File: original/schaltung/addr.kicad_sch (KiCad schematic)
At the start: 6 parts

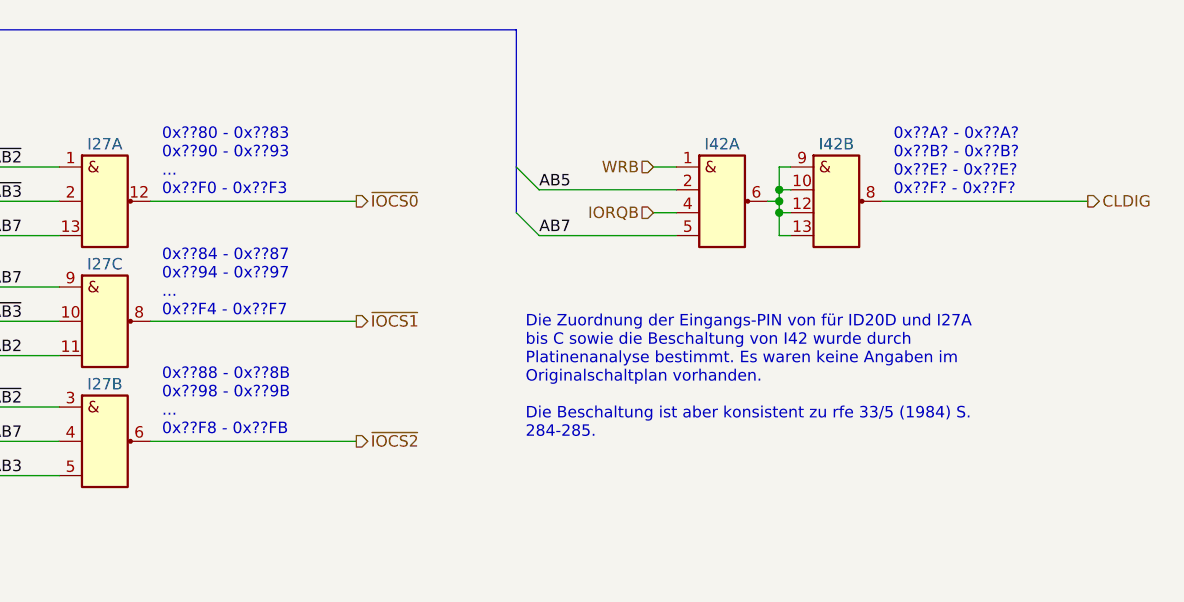
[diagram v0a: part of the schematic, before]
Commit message: I/O-Adressraum auf 8 Bit gekürzt
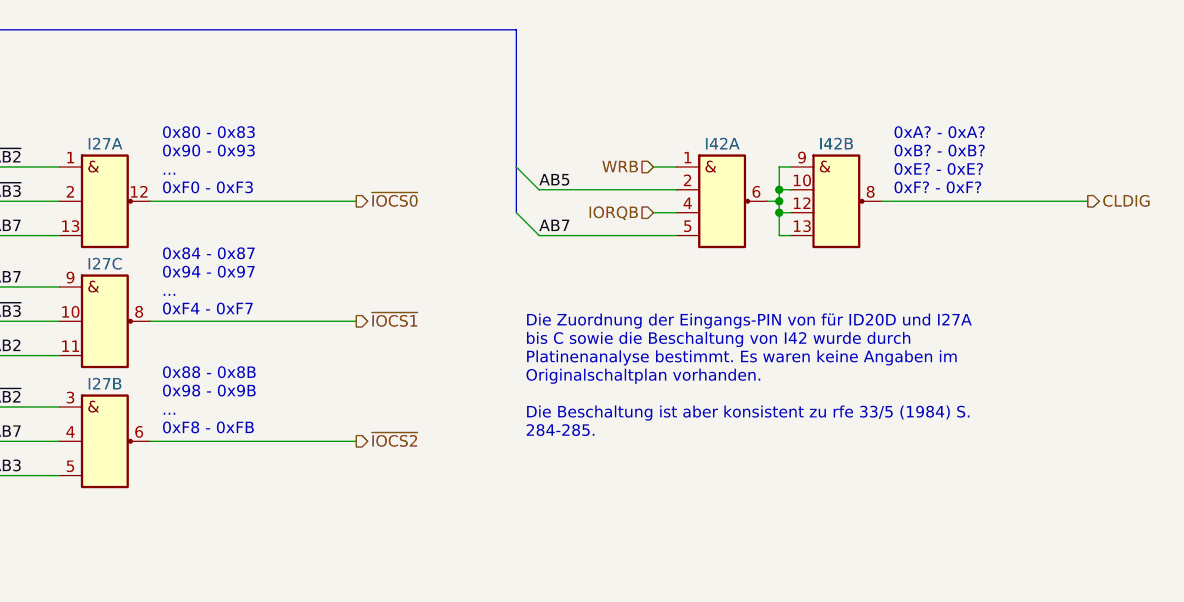
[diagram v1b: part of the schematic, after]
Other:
- note added: "0x80 - 0x83 0x90 - 0x93 ... 0xF0 - 0xF3"
- note added: "0x84 - 0x87 0x94 - 0x97 ... 0xF4 - 0xF7"
- note added: "0x88 - 0x8B 0x98 - 0x9B ... 0xF8 - 0xFB"
- note added: "0xA? - 0xA? 0xB? - 0xB? 0xE? - 0xE? 0xF? - 0xF?"
- note removed: "0x??80 - 0x??83 0x??90 - 0x??93 ... 0x??F0 - 0x??F3"
- note removed: "0x??84 - 0x??87 0x??94 - 0x??97 ... 0x??F4 - 0x??F7"
- note removed: "0x??88 - 0x??8B 0x??98 - 0x??9B ... 0x??F8 - 0x??FB"
- note removed: "0x??A? - 0x??A? 0x??B? - 0x??B? 0x??E? - 0x??E? 0x??F? - 0x??F?"
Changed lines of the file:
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@@
     (effects (font (size 1.27 1.27)) (justify left bottom))
   )
-  (text "0x??84 - 0x??87\n0x??94 - 0x??97\n...\n0x??F4 - 0x??F7"
-    (at 153.67 62.484 0)
+  (text "0x84 - 0x87\n0x94 - 0x97\n...\n0xF4 - 0xF7" (at 153.67 62.484 0)
     (effects (font (size 1.27 1.27)) (justify left bottom))
   )
@@
     (effects (font (size 1.27 1.27)) (justify left bottom))
   )
-  (text "0x??A? - 0x??A?\n0x??B? - 0x??B?\n0x??E? - 0x??E?\n0x??F? - 0x??F?"
-    (at 234.95 49.022 0)
+  (text "0xA? - 0xA?\n0xB? - 0xB?\n0xE? - 0xE?\n0xF? - 0xF?" (at 234.95 49.022 0)
     (effects (font (size 1.27 1.27)) (justify left bottom))
   )
-  (text "0x??80 - 0x??83\n0x??90 - 0x??93\n...\n0x??F0 - 0x??F3"
-    (at 153.67 49.022 0)
+  (text "0x80 - 0x83\n0x90 - 0x93\n...\n0xF0 - 0xF3" (at 153.67 49.022 0)
     (effects (font (size 1.27 1.27)) (justify left bottom))
   )
-  (text "0x??88 - 0x??8B\n0x??98 - 0x??9B\n...\n0x??F8 - 0x??FB"
-    (at 153.67 75.692 0)
+  (text "0x88 - 0x8B\n0x98 - 0x9B\n...\n0xF8 - 0xFB" (at 153.67 75.692 0)
     (effects (font (size 1.27 1.27)) (justify left bottom))
   )
